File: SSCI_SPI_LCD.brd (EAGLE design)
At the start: 114 x 100 mm, 29 parts, among them IC3 74LVC541_RGY, X1 TSW-108-02-S-S, X2 TSW-108-02-S-S

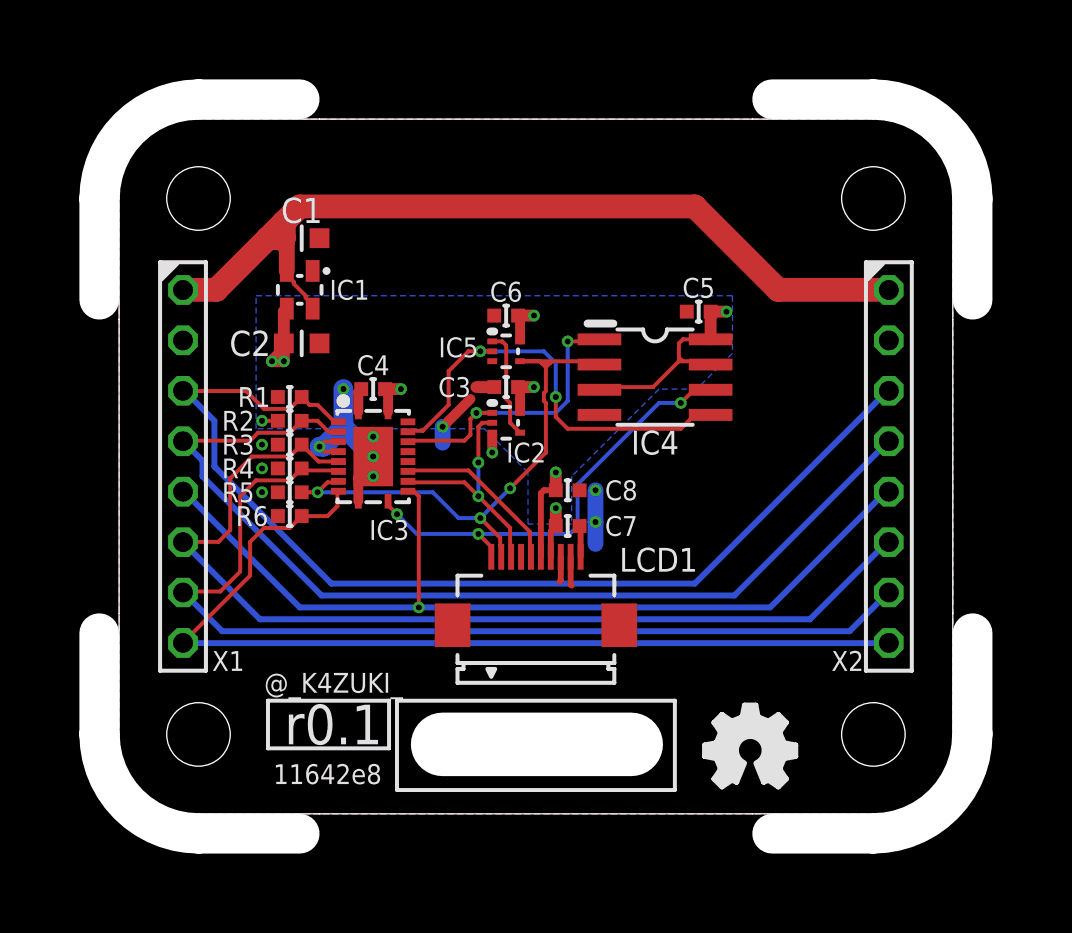
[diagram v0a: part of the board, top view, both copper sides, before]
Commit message: not Dimension but tRestrict/bRestrict to cut copper pour
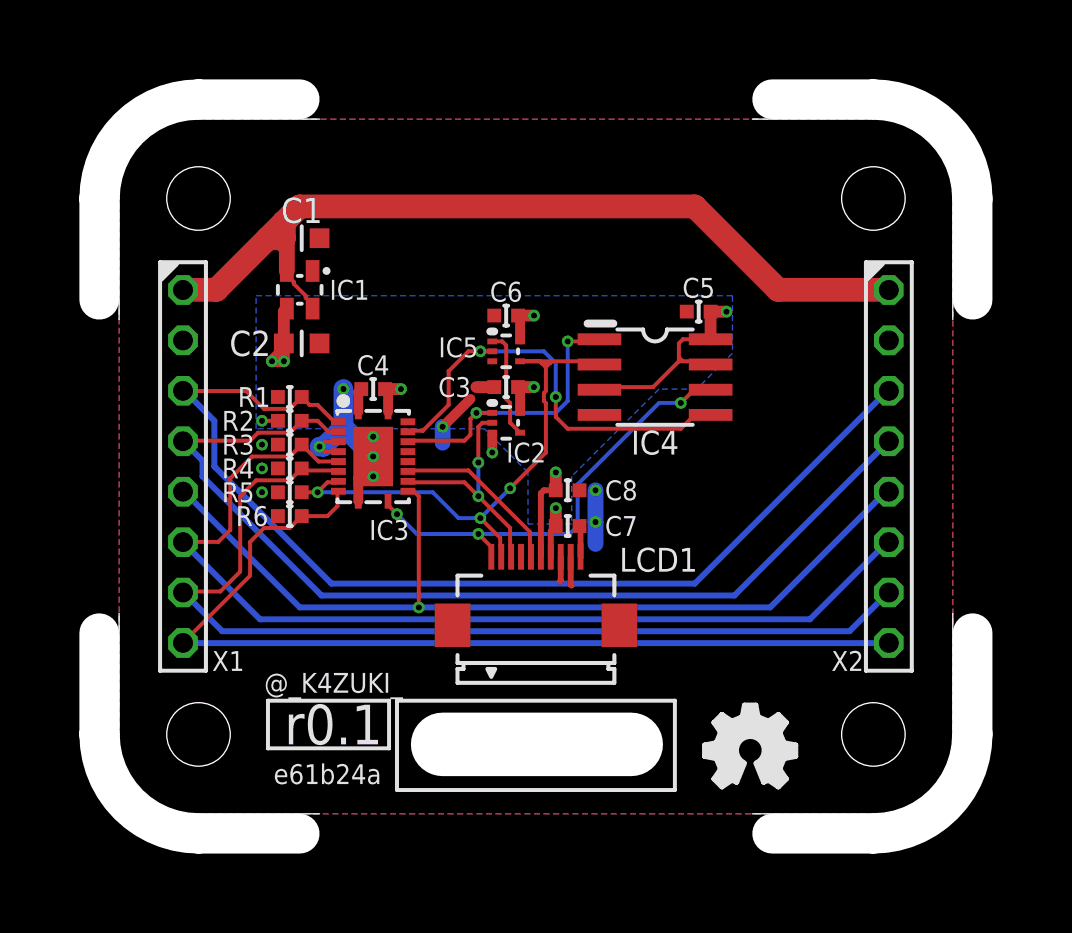
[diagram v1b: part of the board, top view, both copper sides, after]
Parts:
- GIT1: value 11642e8 -> e61b24a
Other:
- outline, holes or cut-outs redrawn
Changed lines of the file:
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@@
 <layer number="40" name="bKeepout" color="1" fill="11" visible="no" active="yes"/>
 <layer number="41" name="tRestrict" color="4" fill="10" visible="yes" active="yes"/>
-<layer number="42" name="bRestrict" color="1" fill="10" visible="no" active="yes"/>
+<layer number="42" name="bRestrict" color="1" fill="10" visible="yes" active="yes"/>
 <layer number="43" name="vRestrict" color="2" fill="10" visible="no" active="yes"/>
 <layer number="44" name="Drills" color="7" fill="1" visible="no" active="yes"/>
-<layer number="45" name="Holes" color="7" fill="1" visible="no" active="yes"/>
+<layer number="45" name="Holes" color="7" fill="1" visible="yes" active="yes"/>
 <layer number="46" name="Milling" color="3" fill="0" visible="yes" active="yes"/>
 <layer number="47" name="Measures" color="7" fill="1" visible="no" active="yes"/>
@@
 <dimension x1="0" y1="0" x2="0" y2="100" x3="-12.6" y3="50" textsize="2" textratio="20" layer="47" dtype="vertical"/>
 <text x="20.8" y="16.6" size="1" layer="21" ratio="20" align="center">@_K4ZUKI_</text>
-<wire x1="20.1" y1="45" x2="41.9" y2="45" width="0" layer="20"/>
-<wire x1="52" y1="34.9" x2="52" y2="20.1" width="0" layer="20"/>
-<wire x1="20.1" y1="10" x2="41.9" y2="10" width="0" layer="20"/>
-<wire x1="10" y1="34.9" x2="10" y2="20.1" width="0" layer="20"/>
+<wire x1="10.2" y1="44.8" x2="51.8" y2="44.8" width="0.4" layer="41"/>
+<wire x1="10.2" y1="44.8" x2="51.8" y2="44.8" width="0.4" layer="42"/>
+<wire x1="10.2" y1="44.8" x2="10.2" y2="10.2" width="0.4" layer="41"/>
+<wire x1="10.2" y1="10.2" x2="51.8" y2="10.2" width="0.4" layer="41"/>
+<wire x1="51.8" y1="10.2" x2="51.8" y2="44.8" width="0.4" layer="41"/>
+<wire x1="10.2" y1="44.8" x2="10.2" y2="10.2" width="0.4" layer="42"/>
+<wire x1="10.2" y1="10.2" x2="51.8" y2="10.2" width="0.4" layer="42"/>
+<wire x1="51.8" y1="10.2" x2="51.8" y2="44.8" width="0.4" layer="42"/>
 </plain>
 <attributes>
@@
 <attribute name="NOT_COMPONENT" value="YES" x="14" y="14" size="1.778" layer="27" rot="R270" display="off"/>
 </element>
-<element name="GIT1" library="git-revision" package="GIT-REVISION" value="11642e8" x="20.5" y="12" smashed="yes">
+<element name="GIT1" library="git-revision" package="GIT-REVISION" value="e61b24a" x="20.5" y="12" smashed="yes">
 <attribute name="NOT_COMPONENT" value="YES" x="20.5" y="12" size="1.778" layer="27" display="off"/>
 <attribute name="VALUE" x="20.5" y="12" size="1" layer="21" ratio="20" align="center"/>

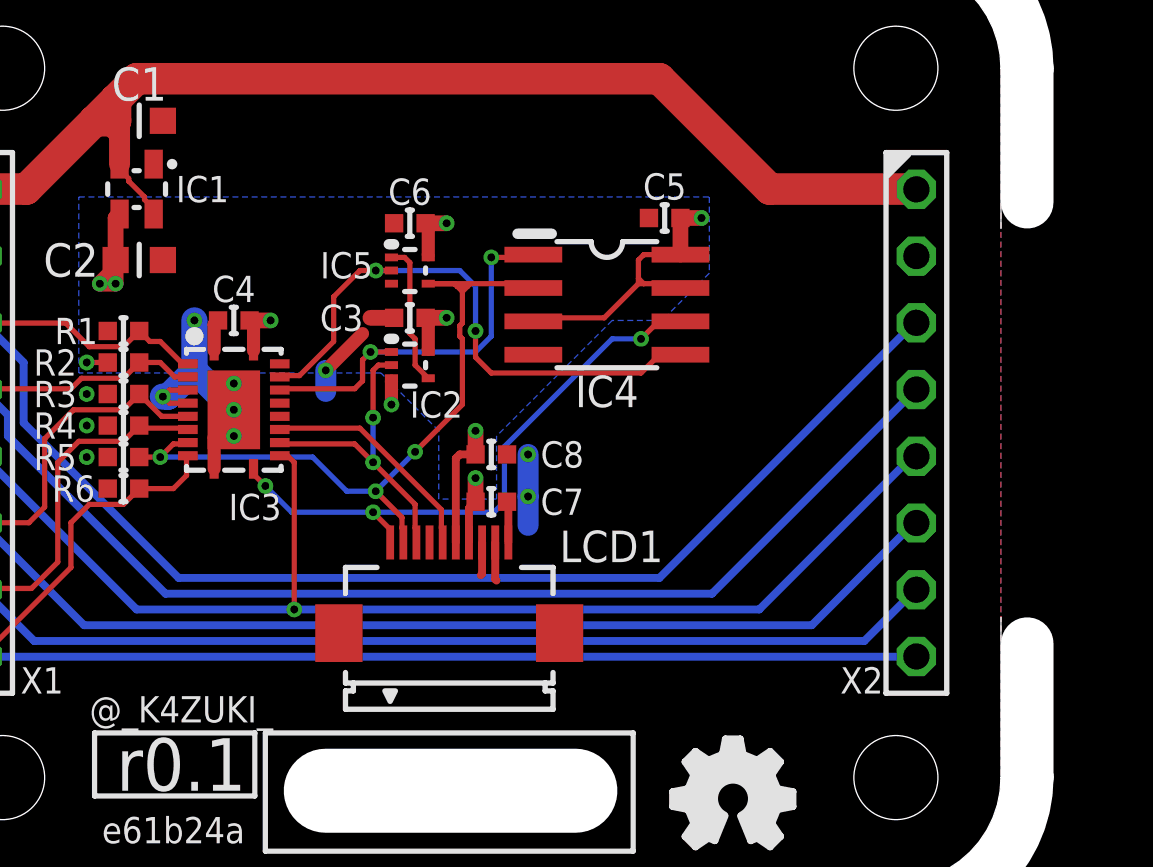
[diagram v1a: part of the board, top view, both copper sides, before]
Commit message: better routing; library update
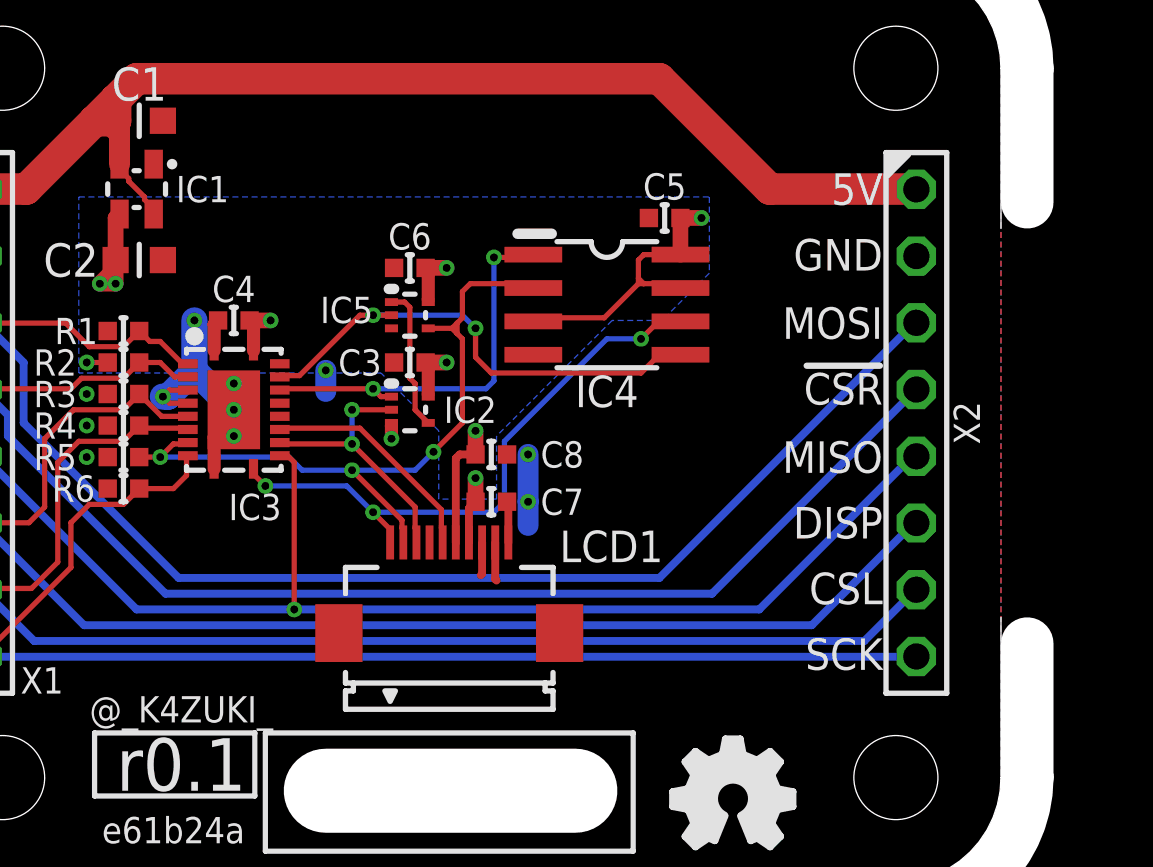
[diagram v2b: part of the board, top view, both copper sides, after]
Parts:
- moved C6 1.70 mm to (29.5, 33.4)
- moved C3 1.70 mm to (29.5, 29.8)
- moved IC2 1.70 mm to (29.5, 28.0)
- moved IC5 1.70 mm to (29.5, 31.6)
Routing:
- net GND: track 22.6 -> 19.3 mm
- net MOSI-: track 22.0 -> 18.8 mm
- net CSL-: track 11.9 -> 10.3 mm
- net MISO-: track 28.6 -> 27.6 mm
- net !CSR!-: track 14.9 -> 15.6 mm
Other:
- board text added: "!CSR!"
- board text added: "5V"
- board text added: "CSL"
- board text added: "DISP"
- board text added: "GND"
- board text added: "MISO"
- board text added: "MOSI"
- board text added: "SCK"

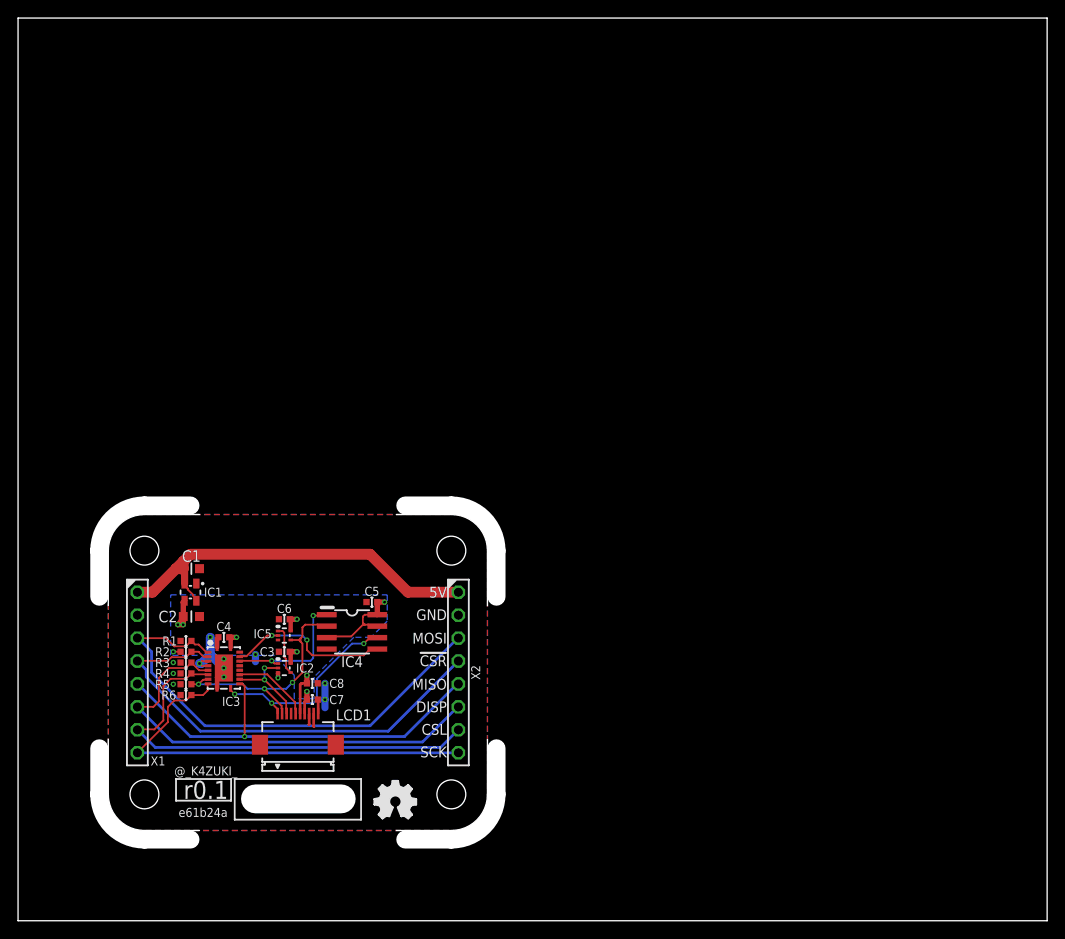
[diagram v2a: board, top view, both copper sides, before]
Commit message: Board size get narrower by 2mm; related moves; library updates
Board size:
42x35mm -> 40x35mm
Moves:
- X1/2 connectors
- CR and ICs
- Version/Revision/Names silk
- OSHW icon silk
library update
- GIT-REVISION -> GIT-REVISION_1.2
- ICON_REVISION_1.2 -> ICON_REVISION_1.7
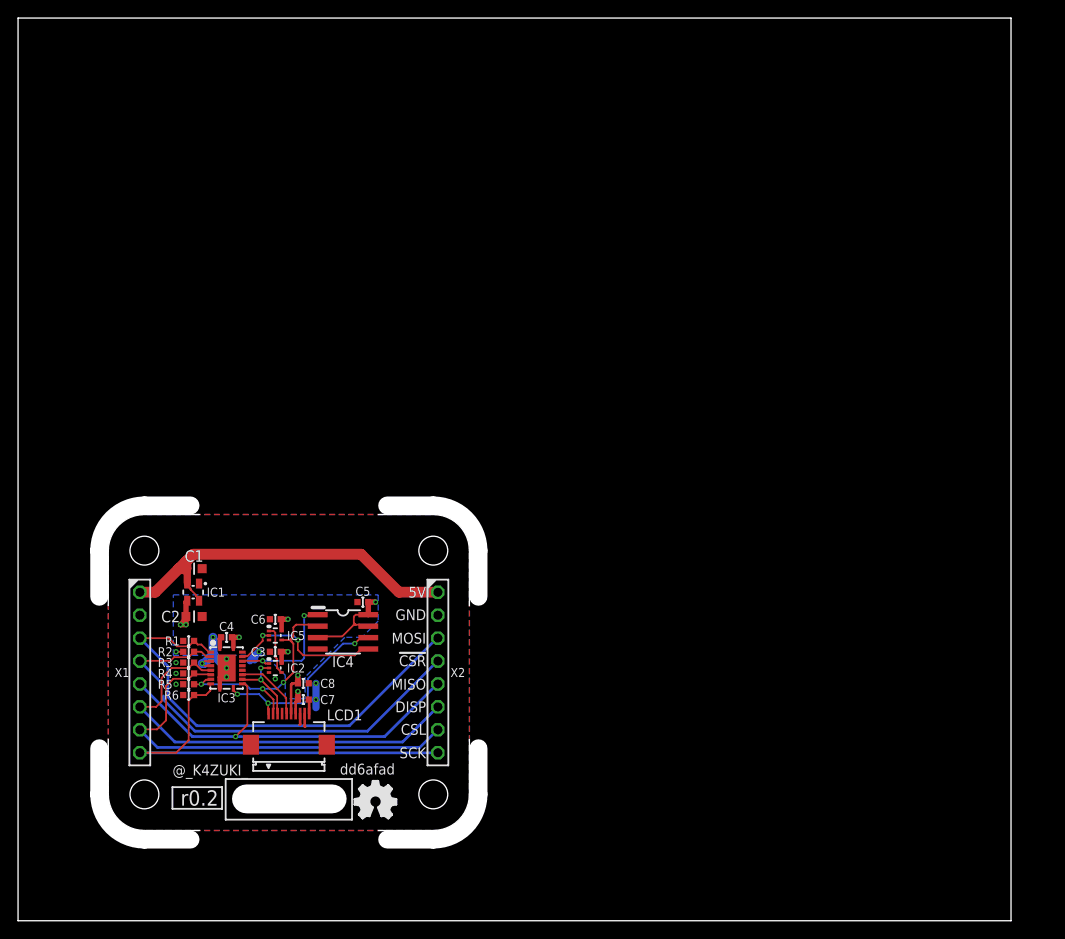
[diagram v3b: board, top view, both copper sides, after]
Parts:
- GIT1: value e61b24a -> dd6afad; device git-revision:GIT-REVISION -> git-revision:GIT-REVISION_1.2
- ICON1: value r0.1 -> r0.2; device mylib:ICON_REVISION2.0 -> mylib:ICON_REVISION1.7
- moved GIT1 18.8 mm to (38.7, 16.8)
- moved X2 2.27 mm to (46.5, 27.5)
- moved ICON2 2.20 mm to (39.6, 13.2)
- moved P1 2.00 mm to (46.0, 14.0)
- moved P2 2.00 mm to (46.0, 41.0)
- moved ICON1 1.08 mm to (20.2, 13.6)
- moved C3 1.00 mm to (28.5, 29.8)
- moved C5 1.00 mm to (38.2, 35.3)
- moved C6 1.00 mm to (28.5, 33.4)
- moved C7 1.00 mm to (31.6, 24.5)
- moved C8 1.00 mm to (31.6, 26.3)
- moved IC2 1.00 mm to (28.5, 28.0)
- moved IC4 1.00 mm to (36.0, 32.0)
- moved IC5 1.00 mm to (28.5, 31.6)
- moved LCD1 1.00 mm to (30.0, 19.5)
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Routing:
- net !CSR!: track 51.0 -> 47.7 mm
- net CSL: track 50.0 -> 47.4 mm
- net 5V: track 46.0 -> 43.4 mm
- net DISP: track 50.6 -> 48.0 mm
- net MISO: track 46.7 -> 44.6 mm
- net MOSI: track 54.0 -> 52.1 mm
- net MISO-: track 27.6 -> 26.0 mm
- net SCK-: track 22.9 -> 21.3 mm
- net CSL-: track 10.3 -> 8.79 mm
- net !CSR!-: track 15.6 -> 14.3 mm
- net DISP-: track 8.73 -> 7.72 mm
- net MOSI-: track 18.8 -> 17.8 mm
- net SCK: track 48.0 -> 47.0 mm
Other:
- board size 114 x 100 mm -> 110 x 100 mm
